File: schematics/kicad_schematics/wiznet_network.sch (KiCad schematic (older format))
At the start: 50 parts

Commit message: added some eval stuff
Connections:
- net labels added: ADDR0, ADDR1, ADDR2, ADDR3, ADDR4, ADDR5, ADDR6, ADDR7, ADDR8, ADDR9, DATA0, DATA1, DATA10, DATA11, DATA12, DATA13, DATA14, DATA15, DATA2, DATA3, DATA4, DATA5, DATA6, DATA7, DATA8, DATA9
- net labels removed: AD0, AD1, AD2, AD3, AD4, AD5, AD6, AD7, AD8, AD9, D0, D1, D10, D11, D12, D13, D14, D15, D2, D3, D4, D5, D6, D7, D8, D9
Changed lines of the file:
@@
-EESchema Schematic File Version 2  date Sat 06 Feb 2010 02:58:11 PM EST
-LIBS:bearboard-cache
+EESchema Schematic File Version 2  date Thu 18 Feb 2010 09:31:45 PM EST
 LIBS:power
 LIBS:device
@@
 LIBS:wiznet
 LIBS:dips-s
+LIBS:bearboard-cache
 EELAYER 24  0
 EELAYER END
@@
 Sheet 2 2
 Title ""
-Date ""
+Date "19 feb 2010"
 Rev ""
 Comp ""
@@
 Text HLabel 2100 2150 0    60   Input ~ 0
 /RESET
-Text HLabel 2100 6200 0    60   Input ~ 0
+Text HLabel 2100 6200 0    60   Output ~ 0
 BRDY3
-Text HLabel 2100 6100 0    60   Input ~ 0
+Text HLabel 2100 6100 0    60   Output ~ 0
 BRDY2
-Text HLabel 2100 6000 0    60   Input ~ 0
+Text HLabel 2100 6000 0    60   Output ~ 0
 BRDY1
-Text HLabel 2100 5900 0    60   Input ~ 0
+Text HLabel 2100 5900 0    60   Output ~ 0
 BRDY0
-Text HLabel 2100 5700 0    60   Input ~ 0
+Text HLabel 2100 5700 0    60   Output ~ 0
 /INT
 Text HLabel 2100 5400 0    60   Input ~ 0
@@
 Entry Wire Line
 	2000 4100 2100 4200
-Text HLabel 1200 2400 0    60   Input ~ 0
+Text HLabel 1200 2400 0    60   BiDi ~ 0
 DATA
 Entry Wire Line
@@
 BIT16EN
 Text Label 2300 3300 0    60   ~ 0
-D7
+DATA7
 Text Label 2300 3400 0    60   ~ 0
-D6
+DATA6
 Text Label 2300 3600 0    60   ~ 0
-D4
+DATA4
 Text Label 2300 3500 0    60   ~ 0
-D5
+DATA5
 Text Label 2300 3900 0    60   ~ 0
-D1
+DATA1
 Text Label 2300 4000 0    60   ~ 0
-D0
+DATA0
 Text Label 2300 3800 0    60   ~ 0
-D2
+DATA2
 Text Label 2300 3700 0    60   ~ 0
-D3
+DATA3
 Text Label 2300 2900 0    60   ~ 0
-D11
+DATA11
 Text Label 2300 3000 0    60   ~ 0
-D10
+DATA10
 Text Label 2300 3200 0    60   ~ 0
-D8
+DATA8
 Text Label 2300 3100 0    60   ~ 0
-D9
+DATA9
 Text Label 2300 2700 0    60   ~ 0
-D13
+DATA13
 Text Label 2300 2800 0    60   ~ 0
-D12
+DATA12
 Text Label 2300 2600 0    60   ~ 0
-D14
+DATA14
 Text Label 2300 2500 0    60   ~ 0
-D15
+DATA15
 Text Label 2300 5100 0    60   ~ 0
-AD0
+ADDR0
 Text Label 2300 4800 0    60   ~ 0
-AD3
+ADDR3
 Text Label 2300 4900 0    60   ~ 0
-AD2
+ADDR2
 Text Label 2300 5000 0    60   ~ 0
-AD1
+ADDR1
 Text Label 2300 4700 0    60   ~ 0
-AD4
+ADDR4
 Text Label 2300 4600 0    60   ~ 0
-AD5
+ADDR5
 Text Label 2300 4500 0    60   ~ 0
-AD6
+ADDR6
 Text Label 2300 4200 0    60   ~ 0
-AD9
+ADDR9
 Text Label 2300 4300 0    60   ~ 0
-AD8
+ADDR8
 Text Label 2300 4400 0    60   ~ 0
-AD7
+ADDR7
 Text Label 2150 5700 0    60   ~ 0
 /INT

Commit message: added more to the schematic
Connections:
- net labels added: A0, A1, A2, A3, A4, A5, A6, A7, A8, A9, A[0..9], D0, D1, D10, D11, D12, D13, D14, D15, D2, D3, D4, D5, D6, D7, D8, D9, D[0..15]
- net labels removed: ADDR, ADDR0, ADDR1, ADDR2, ADDR3, ADDR4, ADDR5, ADDR6, ADDR7, ADDR8, ADDR9, DATA, DATA0, DATA1, DATA10, DATA11, DATA12, DATA13, DATA14, DATA15, DATA2, DATA3, DATA4, DATA5, DATA6, DATA7, DATA8, DATA9
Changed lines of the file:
@@
-EESchema Schematic File Version 2  date Fri 19 Feb 2010 01:22:01 AM EST
+EESchema Schematic File Version 2  date Fri 19 Feb 2010 09:12:18 AM EST
 LIBS:power
 LIBS:device
@@
 LIBS:dips-s
 LIBS:misc
+LIBS:usb-b
 LIBS:bearboard-cache
 EELAYER 24  0
 EELAYER END
 $Descr B 17000 11000
-Sheet 2 2
+Sheet 2 3
 Title ""
 Date "19 feb 2010"
@@
 /WR
 Text HLabel 1400 4100 0    60   Input ~ 0
-ADDR
+A[0..9]
 Wire Bus Line
 	1400 4100 2000 4100
@@
 	2000 4100 2100 4200
 Text HLabel 1200 2400 0    60   BiDi ~ 0
-DATA
+D[0..15]
 Entry Wire Line
 	2000 3900 2100 4000
@@
 BIT16EN
 Text Label 2300 3300 0    60   ~ 0
-DATA7
+D7
 Text Label 2300 3400 0    60   ~ 0
-DATA6
+D6
 Text Label 2300 3600 0    60   ~ 0
-DATA4
+D4
 Text Label 2300 3500 0    60   ~ 0
-DATA5
+D5
 Text Label 2300 3900 0    60   ~ 0
-DATA1
+D1
 Text Label 2300 4000 0    60   ~ 0
-DATA0
+D0
 Text Label 2300 3800 0    60   ~ 0
-DATA2
+D2
 Text Label 2300 3700 0    60   ~ 0
-DATA3
+D3
 Text Label 2300 2900 0    60   ~ 0
-DATA11
+D11
 Text Label 2300 3000 0    60   ~ 0
-DATA10
+D10
 Text Label 2300 3200 0    60   ~ 0
-DATA8
+D8
 Text Label 2300 3100 0    60   ~ 0
-DATA9
+D9
 Text Label 2300 2700 0    60   ~ 0
-DATA13
+D13
 Text Label 2300 2800 0    60   ~ 0
-DATA12
+D12
 Text Label 2300 2600 0    60   ~ 0
-DATA14
+D14
 Text Label 2300 2500 0    60   ~ 0
-DATA15
+D15
 Text Label 2300 5100 0    60   ~ 0
-ADDR0
+A0
 Text Label 2300 4800 0    60   ~ 0
-ADDR3
+A3
 Text Label 2300 4900 0    60   ~ 0
-ADDR2
+A2
 Text Label 2300 5000 0    60   ~ 0
-ADDR1
+A1
 Text Label 2300 4700 0    60   ~ 0
-ADDR4
+A4
 Text Label 2300 4600 0    60   ~ 0
-ADDR5
+A5
 Text Label 2300 4500 0    60   ~ 0
-ADDR6
+A6
 Text Label 2300 4200 0    60   ~ 0
-ADDR9
+A9
 Text Label 2300 4300 0    60   ~ 0
-ADDR8
+A8
 Text Label 2300 4400 0    60   ~ 0
-ADDR7
+A7
 Text Label 2150 5700 0    60   ~ 0
 /INT

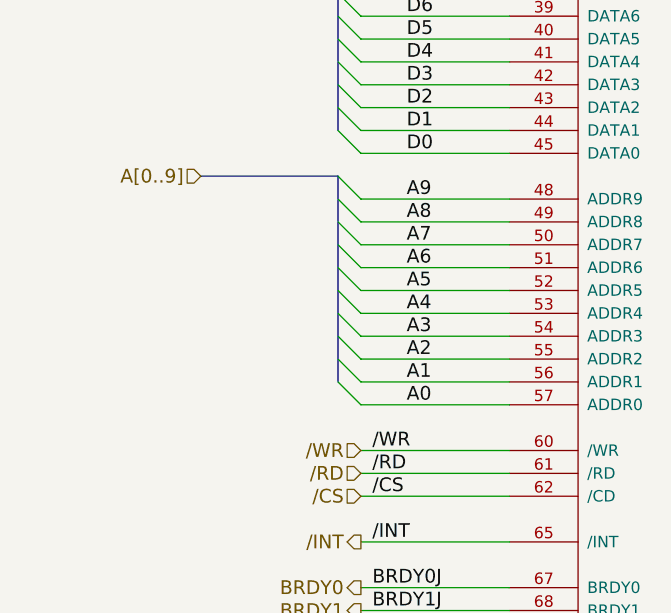
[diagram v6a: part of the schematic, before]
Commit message: Added JTAG connector & Modified Wiznet Schematic Changed A[0-8] = A[1-9]
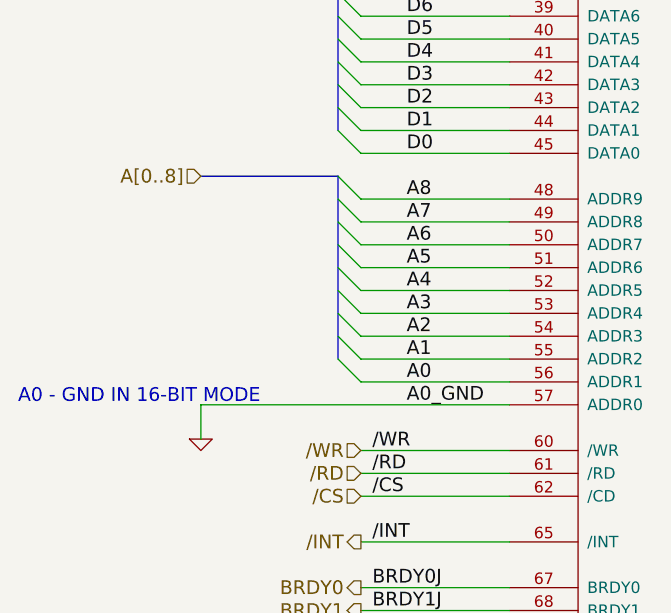
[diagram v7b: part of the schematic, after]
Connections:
- net labels added: A0_GND, A[0..8]
- net labels removed: A9, A[0..9]
- wire segments 193 -> 194
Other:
- note added: "A0 - GND IN 16-BIT MODE"

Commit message: Added Power connections, JTAG, TRACE, and some notes to the schematics
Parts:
- C?: value 0.1uF -> 10uF
- C?: value 10uF/16V -> 3.3uF_Tant; TypeOfCap (none) -> Tant
- C? (x3): TypeOfCap (none) -> Tant
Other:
- note added: "Make analogue ground plane as wide as possible when designing\nthe PCB layout.\nDigital ground\nMake digital ground plane as wide as possible when designing the"
- note added: "Recommend for power design.\n1. Locate decoupling capacitor as close as possible to W5300.\n2. Use ground plane as wide as possible.\n3. If ground plane width is adequate, having a separate analog ground plane and digital\nground plane is good practice.\nIf ground plane is not wide, design analog and digital ground planes as a single ground plane,\nrather than separate them."
- note added: "Recommend for the better performance.\n1. MII interface signal line length should not be more than 25cm if possible.\n2. The length of MII_TXD[3:0] should be same if possible.\n3. The length of MII_RXD[3:0] should be same if possible.\n4. The length of MII_TXC should not be longer than MII_TXD[3:0] signal line by 2.5cm.\n5. The length of MII_RXC should not be longer than MII_RXD[3:0] signal line 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"
- note added: "Refer to “Clock Characteristic” of “7.Electrical Specifications”\nThese can be used for internal PHY mode(TEST_MODE[3:0]=”0000”) or\nexternal PHY mode with crystal clock (TEST_MODE[3:0]=”0001”).\nWhen using oscillator at the internal PHY mode, be sure to use 1.8V level\noscillator and connect only to XTLP. And let be float XTLN."
